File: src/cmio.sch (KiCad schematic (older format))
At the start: 34 parts, among them J1 USB_POWER, J2 BANK0, J3 USB_OTG, J4 CM3Lite, J5 TVOUT, J6 BANK1, J7 Micro_SD_Card_TFP09_2_12B, SW1 Reset, U1 AP3417B, U2 AP3417B, U3 SP6203EM5-L-2-8/TR, U4 AP2401

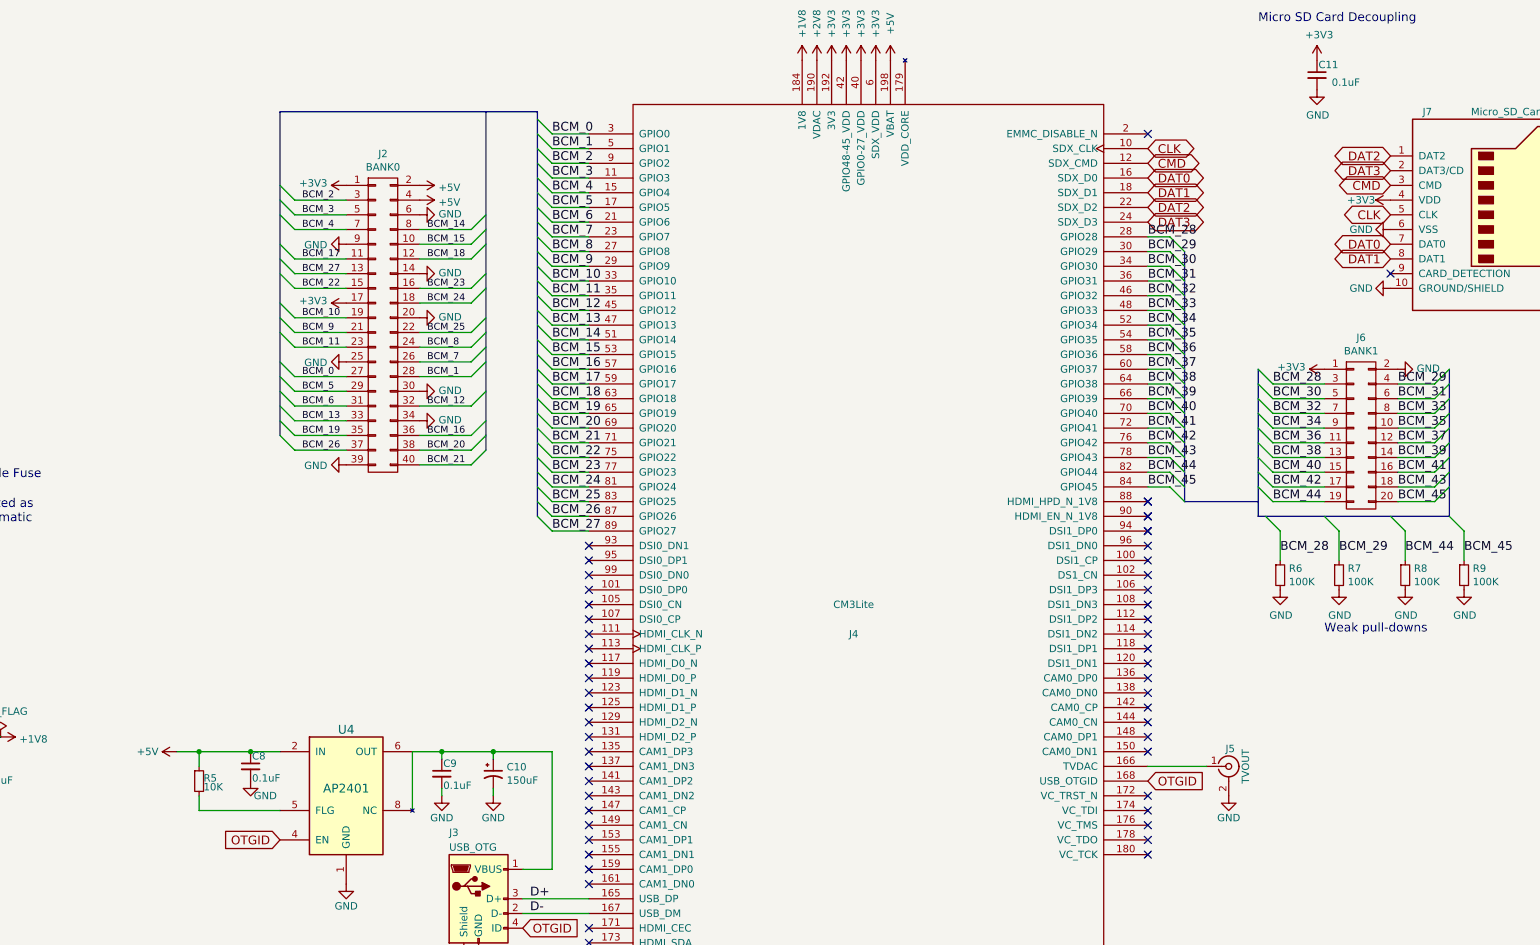
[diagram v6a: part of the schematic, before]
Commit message: Remove compatibility with RPi for simpler design
Signed-off-by: Mahyar Koshkouei <mahyar.koshkouei@gmail.com>
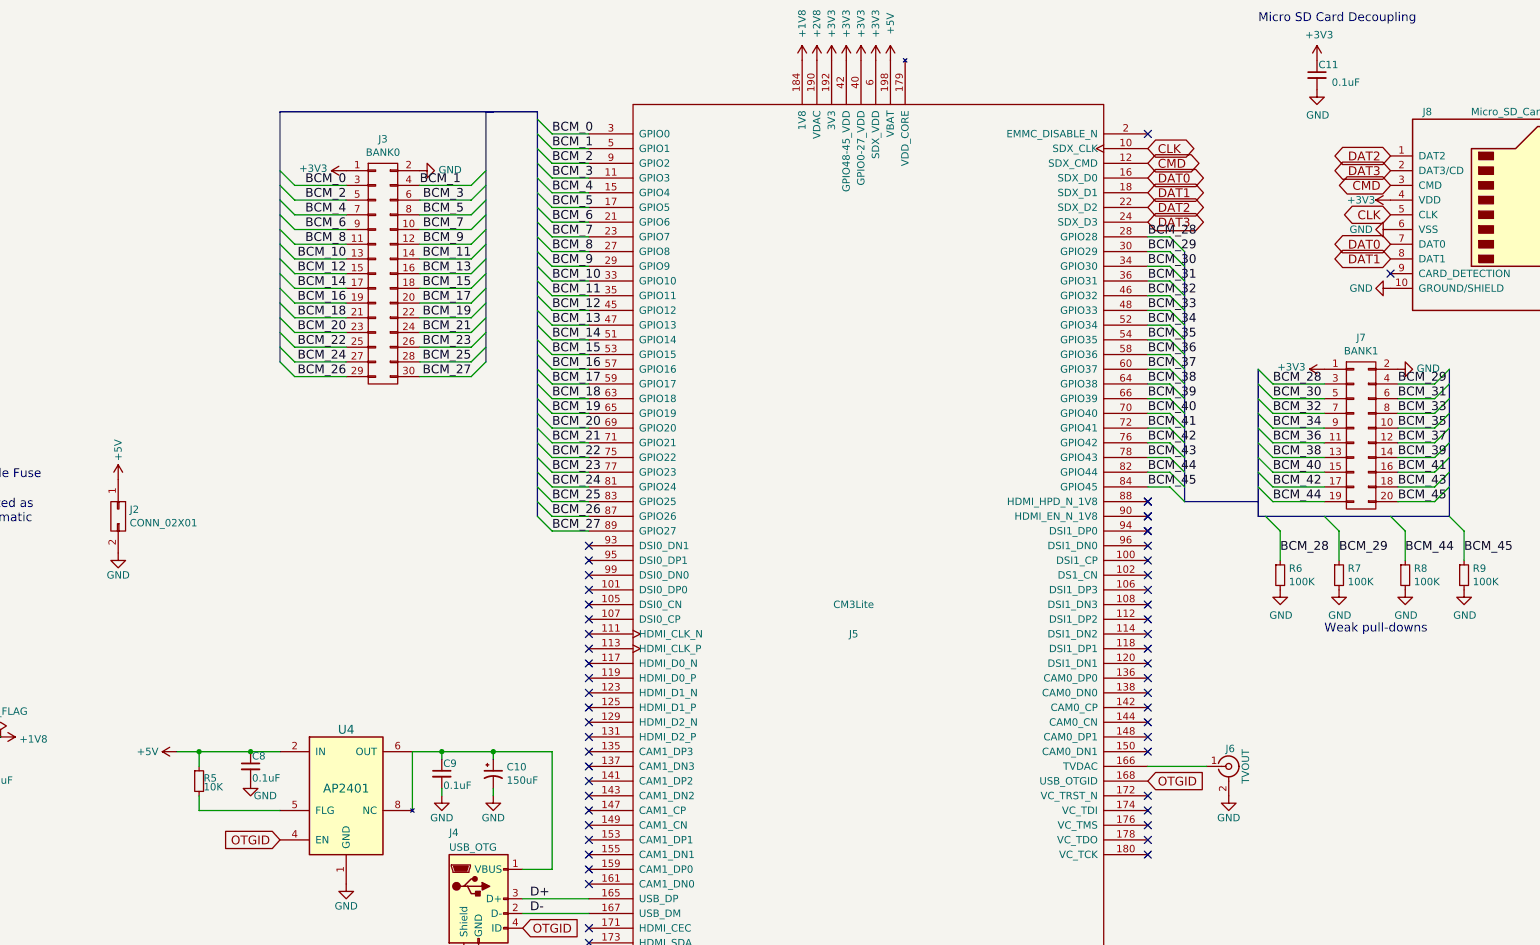
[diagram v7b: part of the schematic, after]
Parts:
- removed J2: BANK0, Pin_Headers:Pin_Header_Straight_2x20_Pitch2.54mm, symbol CONN_02X20
- added J2: CONN_02X01, Pin_Headers:Pin_Header_Straight_2x01_Pitch2.54mm_SMD, symbol CONN_02X01
- added J3: BANK0, Pin_Headers:Pin_Header_Straight_2x15_Pitch2.54mm_SMD, symbol CONN_02X15
- J7: renamed from J6; footprint Pin_Headers:Pin_Header_Straight_2x10_Pitch2.54mm -> Pin_Headers:Pin_Header_Straight_2x10_Pitch2.54mm_SMD
- renumbered J3 to J4, J4 to J5, J5 to J6, J7 to J8
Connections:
- net +3V3: now also J3.1 (P1)
- net +5V: now also J2.1 (P1)
- net BCM_0: now also J3.3 (P3)
- net BCM_1: now also J3.4 (P4)
- net BCM_10: now also J3.13 (P13)
- net BCM_11: now also J3.14 (P14)
- net BCM_12: now also J3.15 (P15)
- net BCM_13: now also J3.16 (P16)
- net BCM_14: now also J3.17 (P17)
- net BCM_15: now also J3.18 (P18)
- net BCM_16: now also J3.19 (P19)
- net BCM_17: now also J3.20 (P20)
- net BCM_18: now also J3.21 (P21)
- net BCM_19: now also J3.22 (P22)
- net BCM_2: now also J3.5 (P5)
- net BCM_20: now also J3.23 (P23)
- net BCM_21: now also J3.24 (P24)
- net BCM_22: now also J3.25 (P25)
- net BCM_23: now also J3.26 (P26)
- net BCM_24: now also J3.27 (P27)
- net BCM_25: now also J3.28 (P28)
- net BCM_26: now also J3.29 (P29)
- net BCM_27: now also J3.30 (P30)
- net BCM_3: now also J3.6 (P6)
- net BCM_4: now also J3.7 (P7)
- net BCM_5: now also J3.8 (P8)
- net BCM_6: now also J3.9 (P9)
- net BCM_7: now also J3.10 (P10)
- net BCM_8: now also J3.11 (P11)
- net BCM_9: now also J3.12 (P12)
- net GND: now also J2.2 (P2), J3.2 (P2)

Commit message: Complete routing
Signed-off-by: Mahyar Koshkouei <mahyar.koshkouei@gmail.com>
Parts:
- removed J2: CONN_02X01, Pin_Headers:Pin_Header_Straight_2x01_Pitch2.54mm_SMD, symbol CONN_02X01
- added C12: 47uF, Capacitors_Tantalum_SMD:CP_Tantalum_Case-A_EIA-3216-18_Hand, symbol CP1_Small
- C10: value 150uF -> 47uF; footprint Capacitors_SMD:CP_Elec_6.3x7.7 -> Capacitors_Tantalum_SMD:CP_Tantalum_Case-A_EIA-3216-18_Hand
- J1, J4: footprint foot:Micro_USB_B_10104110 -> foot:Molex_Right_Angle_SMT_TypeB_MicroUSB_105017
- J3: footprint Pin_Headers:Pin_Header_Straight_2x15_Pitch2.54mm_SMD -> Pin_Headers:Pin_Header_Straight_2x15_Pitch2.54mm
- J5: footprint foot:CM3_Socket_SODIMM_DDR1-2_TE_1612618 -> foot:CM3_Socket_SODIMM_DDR1-2_TE_1612618_NoHole
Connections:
- net +5V: now also C12.1
- net GND: now also C12.2
